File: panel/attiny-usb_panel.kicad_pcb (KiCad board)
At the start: 2 copper layers, 83 x 52.6 mm, 79 parts, among them J1 Conn_01x05, J2 Conn_01x05, J3 Conn_01x05, U1 ATtiny85-20P, U3 ATtiny85-20P, U5 ATtiny85-20P

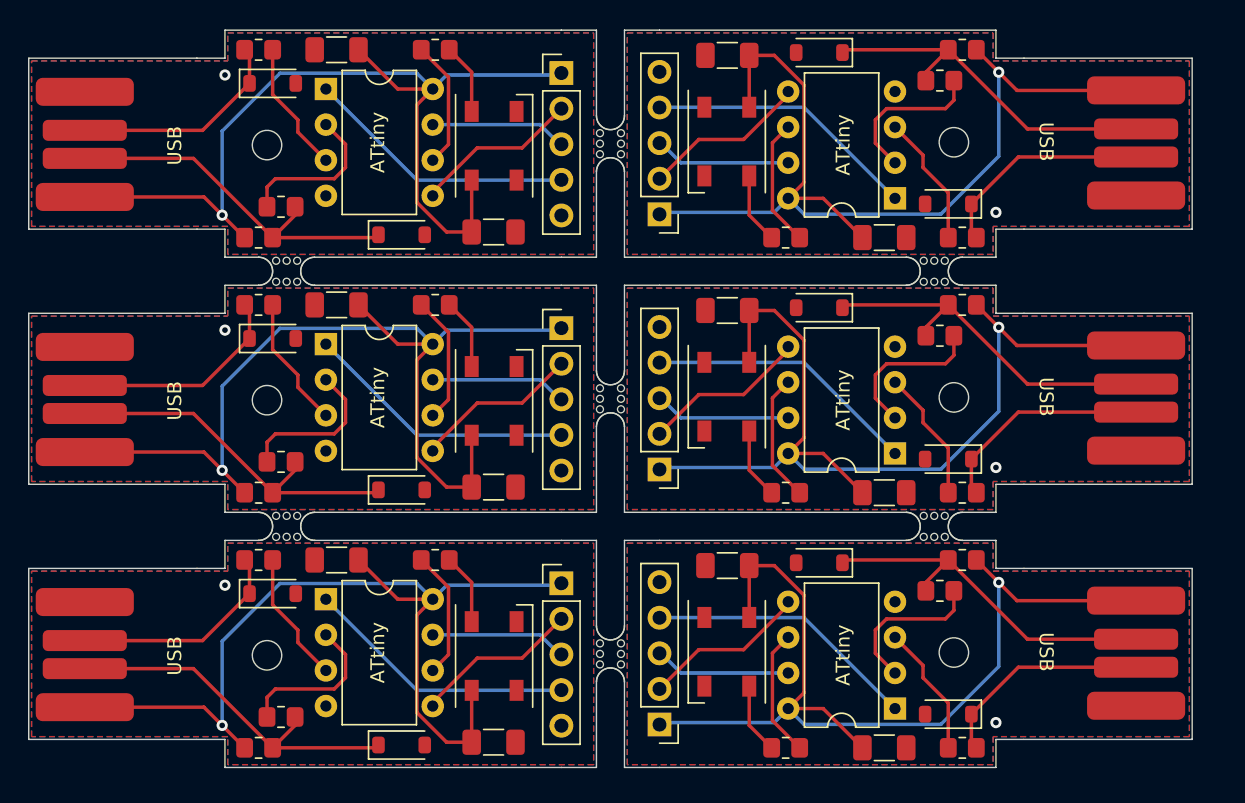
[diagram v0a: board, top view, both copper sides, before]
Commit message: create panel of 2x3
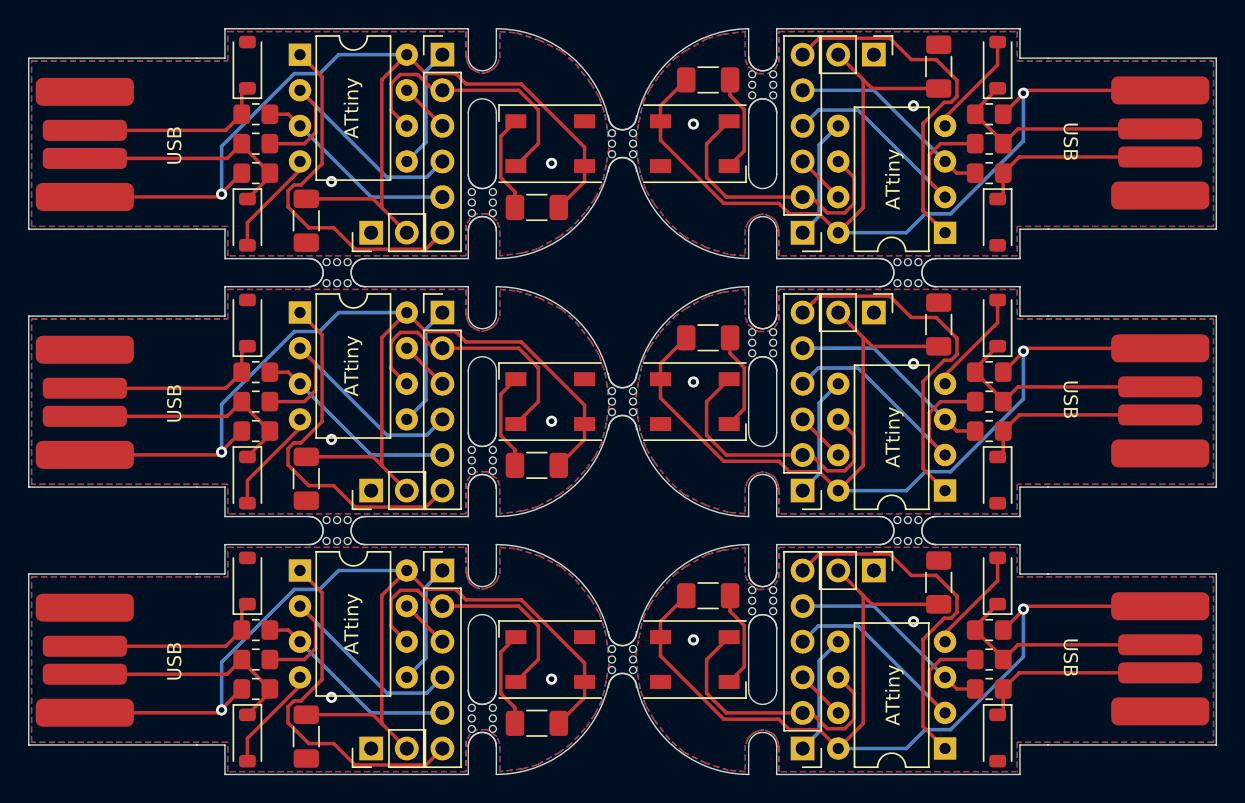
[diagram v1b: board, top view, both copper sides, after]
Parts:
- removed the C3 at (122.0, 117.6)
- removed the C3 at (161.0, 131.0)
- removed the C4 at (149.8, 118.0)
- removed the C4 at (133.2, 130.6)
- removed the C5 at (161.0, 112.8)
- removed the C5 at (122.0, 135.8)
- removed the C6 at (133.2, 148.8)
- removed the C6 at (149.8, 99.8)
- removed the D4 at (126.6, 130.8)
- removed the D4 at (156.4, 117.8)
- removed the D5 at (117.4, 120.0)
- removed the D5 at (165.6, 128.6)
- removed the D6 at (133.2, 124.5)
- removed the D6 at (149.8, 124.2)
- removed the D7 at (156.4, 99.6)
- removed the D7 at (126.6, 149.0)
- removed the D8 at (117.4, 138.2)
- removed the D8 at (165.6, 110.4)
- removed the D9 at (149.8, 106.0)
- removed the D9 at (133.2, 142.7)
- removed J1 (x2): Conn_01x05, Connector_PinHeader_2.54mm:PinHeader_1x05_P2.54mm_Vertical
- removed the J2 at (145.0, 129.3)
- removed the J2 at (138.0, 119.3)
- removed the J3 at (138.0, 137.5)
- removed the J3 at (145.0, 111.1)
- removed R10 (x2): 68R, Resistor_SMD:R_0805_2012Metric_Pad1.20x1.40mm_HandSolder
- removed R11 (x2): 400R, Resistor_SMD:R_0805_2012Metric_Pad1.20x1.40mm_HandSolder
- removed R12 (x2): 1k5, Resistor_SMD:R_0805_2012Metric_Pad1.20x1.40mm_HandSolder
- removed the R3 at (154.0, 149.2)
- removed the R3 at (129.0, 99.4)
- removed the R5 at (166.6, 131.0)
- removed the R5 at (116.4, 117.6)
- removed the R6 at (118.0, 128.8)
- removed the R6 at (165.0, 119.8)
- removed the R7 at (154.0, 131.0)
- removed the R7 at (129.0, 117.6)
- removed the R8 at (116.4, 131.0)
- removed the R8 at (166.6, 117.6)
- removed the R9 at (116.4, 135.8)
- removed the R9 at (166.6, 112.8)
- removed the U3 at (161.8, 128.2)
- removed the U3 at (121.2, 120.4)
- removed the U4 at (179.0, 124.2)
- removed the U4 at (104.0, 124.3)
- removed the U5 at (121.2, 138.6)
- removed the U5 at (161.8, 110.0)
- removed the U6 at (179.0, 106.0)
- removed the U6 at (104.0, 142.6)
- removed the mouse-bite-2mm-slot at (164.6, 115.2)
- removed the mouse-bite-2mm-slot at (141.5, 142.5)
- removed the mouse-bite-2mm-slot at (118.4, 133.4)
- removed the mouse-bite-2mm-slot at (118.4, 115.2)
- removed the mouse-bite-2mm-slot at (141.5, 106.1)
- removed the mouse-bite-2mm-slot at (141.5, 124.3)
- removed the mouse-bite-2mm-slot at (164.6, 133.4)
- added C3: 100n, Capacitor_SMD:C_1206_3216Metric_Pad1.33x1.80mm_HandSolder, F.Cu at (164.9, 119.0)
- added C3: 100n, Capacitor_SMD:C_1206_3216Metric_Pad1.33x1.80mm_HandSolder, F.Cu at (119.8, 130.0)
- added C4: 100n, Capacitor_SMD:C_1206_3216Metric_Pad1.33x1.80mm_HandSolder, F.Cu at (136.2, 129.1)
- added C4: 100n, Capacitor_SMD:C_1206_3216Metric_Pad1.33x1.80mm_HandSolder, F.Cu at (148.5, 120.0)
- added C5: 100n, Capacitor_SMD:C_1206_3216Metric_Pad1.33x1.80mm_HandSolder, F.Cu at (164.9, 100.6)
- added C5: 100n, Capacitor_SMD:C_1206_3216Metric_Pad1.33x1.80mm_HandSolder, F.Cu at (119.8, 148.4)
- added C6: 100n, Capacitor_SMD:C_1206_3216Metric_Pad1.33x1.80mm_HandSolder, F.Cu at (136.2, 147.4)
- added C6: 100n, Capacitor_SMD:C_1206_3216Metric_Pad1.33x1.80mm_HandSolder, F.Cu at (148.5, 101.5)
- added D4: 3V6, Diode_SMD:D_SOD-123, F.Cu at (115.6, 130.1)
- added D4: 3V6, Diode_SMD:D_SOD-123, F.Cu at (169.1, 118.9)
- added D5: 3V6, Diode_SMD:D_SOD-123, F.Cu at (169.1, 130.1)
- added D5: 3V6, Diode_SMD:D_SOD-123, F.Cu at (115.6, 118.9)
- added D6: WS2812B, LED_SMD:LED_SK6812_PLCC4_5.0x5.0mm_P3.2mm, F.Cu at (147.5, 124.5)
- added D6: WS2812B, LED_SMD:LED_SK6812_PLCC4_5.0x5.0mm_P3.2mm, F.Cu at (137.2, 124.5)
- added D7: 3V6, Diode_SMD:D_SOD-123, F.Cu at (169.1, 100.5)
- added D7: 3V6, Diode_SMD:D_SOD-123, F.Cu at (115.6, 148.5)
- added D8: 3V6, Diode_SMD:D_SOD-123, F.Cu at (115.6, 137.3)
- added D8: 3V6, Diode_SMD:D_SOD-123, F.Cu at (169.1, 111.7)
- added D9: WS2812B, LED_SMD:LED_SK6812_PLCC4_5.0x5.0mm_P3.2mm, F.Cu at (147.5, 106.1)
- added D9: WS2812B, LED_SMD:LED_SK6812_PLCC4_5.0x5.0mm_P3.2mm, F.Cu at (137.2, 142.9)
- added J2: Conn_01x06, Connector_PinHeader_2.54mm:PinHeader_1x06_P2.54mm_Vertical, F.Cu at (129.5, 99.8)
- added J2: Conn_01x06, Connector_PinHeader_2.54mm:PinHeader_1x06_P2.54mm_Vertical, F.Cu at (155.2, 149.2)
- added J3: Conn_01x02, Connector_PinHeader_2.54mm:PinHeader_1x02_P2.54mm_Vertical, F.Cu at (124.4, 112.5)
- added J3: Conn_01x02, Connector_PinHeader_2.54mm:PinHeader_1x02_P2.54mm_Vertical, F.Cu at (160.3, 136.6)
- added J4: Conn_01x06, Connector_PinHeader_2.54mm:PinHeader_1x06_P2.54mm_Vertical, F.Cu at (155.2, 130.8)
- added J4: Conn_01x06, Connector_PinHeader_2.54mm:PinHeader_1x06_P2.54mm_Vertical, F.Cu at (129.5, 118.2)
- added J5: Conn_01x02, Connector_PinHeader_2.54mm:PinHeader_1x02_P2.54mm_Vertical, F.Cu at (160.3, 118.2)
- added J5: Conn_01x02, Connector_PinHeader_2.54mm:PinHeader_1x02_P2.54mm_Vertical, F.Cu at (124.4, 130.8)
- added J6: Conn_01x06, Connector_PinHeader_2.54mm:PinHeader_1x06_P2.54mm_Vertical, F.Cu at (155.2, 112.5)
- added J6: Conn_01x06, Connector_PinHeader_2.54mm:PinHeader_1x06_P2.54mm_Vertical, F.Cu at (129.5, 136.6)
- added J7: Conn_01x02, Connector_PinHeader_2.54mm:PinHeader_1x02_P2.54mm_Vertical, F.Cu at (124.4, 149.2)
- added J7: Conn_01x02, Connector_PinHeader_2.54mm:PinHeader_1x02_P2.54mm_Vertical, F.Cu at (160.3, 99.8)
- added R3: 68R, Resistor_SMD:R_0805_2012Metric_Pad1.20x1.40mm_HandSolder, F.Cu at (168.5, 126.6)
- added R3: 68R, Resistor_SMD:R_0805_2012Metric_Pad1.20x1.40mm_HandSolder, F.Cu at (116.2, 122.4)
- added R5: 68R, Resistor_SMD:R_0805_2012Metric_Pad1.20x1.40mm_HandSolder, F.Cu at (116.2, 124.5)
- added R5: 68R, Resistor_SMD:R_0805_2012Metric_Pad1.20x1.40mm_HandSolder, F.Cu at (168.5, 124.5)
- added R6: 1k5, Resistor_SMD:R_0805_2012Metric_Pad1.20x1.40mm_HandSolder, F.Cu at (168.5, 122.4)
- added R6: 1k5, Resistor_SMD:R_0805_2012Metric_Pad1.20x1.40mm_HandSolder, F.Cu at (116.2, 126.6)
- added R7: 68R, Resistor_SMD:R_0805_2012Metric_Pad1.20x1.40mm_HandSolder, F.Cu at (116.2, 140.8)
- added R7: 68R, Resistor_SMD:R_0805_2012Metric_Pad1.20x1.40mm_HandSolder, F.Cu at (168.5, 108.2)
- added R8: 68R, Resistor_SMD:R_0805_2012Metric_Pad1.20x1.40mm_HandSolder, F.Cu at (168.5, 106.1)
- added R8: 68R, Resistor_SMD:R_0805_2012Metric_Pad1.20x1.40mm_HandSolder, F.Cu at (116.2, 142.9)
- added R9: 1k5, Resistor_SMD:R_0805_2012Metric_Pad1.20x1.40mm_HandSolder, F.Cu at (168.5, 104.0)
- added R9: 1k5, Resistor_SMD:R_0805_2012Metric_Pad1.20x1.40mm_HandSolder, F.Cu at (116.2, 145.0)
- added U3: ATtiny85-20P, Package_DIP:DIP-8_W7.62mm, F.Cu at (119.3, 118.2)
- added U3: ATtiny85-20P, Package_DIP:DIP-8_W7.62mm, F.Cu at (165.4, 130.8)
- added U4: ~, my_lib:pcb_usb-connector, F.Cu at (180.7, 124.5)
- added U4: ~, my_lib:pcb_usb-connector, F.Cu at (104.0, 124.5)
- added U5: ATtiny85-20P, Package_DIP:DIP-8_W7.62mm, F.Cu at (165.4, 112.5)
- added U5: ATtiny85-20P, Package_DIP:DIP-8_W7.62mm, F.Cu at (119.3, 136.6)
- added U6: ~, my_lib:pcb_usb-connector, F.Cu at (104.0, 142.9)
- added U6: ~, my_lib:pcb_usb-connector, F.Cu at (180.7, 106.0)
- added mouse-bite-2mm-slot: VAL**, my_lib:mouse-bite-2mm-slot, F.Cu at (152.4, 138.7)
- added mouse-bite-2mm-slot: VAL**, my_lib:mouse-bite-2mm-slot, F.Cu at (162.7, 115.3)
- added mouse-bite-2mm-slot: VAL**, my_lib:mouse-bite-2mm-slot, F.Cu at (132.4, 110.3)
- added mouse-bite-2mm-slot: VAL**, my_lib:mouse-bite-2mm-slot, F.Cu at (162.7, 133.7)
- added mouse-bite-2mm-slot: VAL**, my_lib:mouse-bite-2mm-slot, F.Cu at (122.0, 133.7)
- added mouse-bite-2mm-slot: VAL**, my_lib:mouse-bite-2mm-slot, F.Cu at (122.0, 115.3)
- added mouse-bite-2mm-slot: VAL**, my_lib:mouse-bite-2mm-slot, F.Cu at (142.4, 124.5)
- added mouse-bite-2mm-slot: VAL**, my_lib:mouse-bite-2mm-slot, F.Cu at (142.4, 106.1)
- added mouse-bite-2mm-slot: VAL**, my_lib:mouse-bite-2mm-slot, F.Cu at (142.4, 142.9)
- added mouse-bite-2mm-slot1: VAL**, my_lib:mouse-bite-2mm-slot, F.Cu at (132.4, 128.7)
- added mouse-bite-2mm-slot1: VAL**, my_lib:mouse-bite-2mm-slot, F.Cu at (152.4, 120.3)
- added mouse-bite-2mm-slot2: VAL**, my_lib:mouse-bite-2mm-slot, F.Cu at (132.4, 147.1)
- added mouse-bite-2mm-slot2: VAL**, my_lib:mouse-bite-2mm-slot, F.Cu at (152.4, 101.9)
- D3 (x2): value SK6812 -> WS2812B
- moved D1 12.8 mm to (169.1, 137.3), turned to 90 degrees
- moved C1 12.4 mm to (164.9, 137.4), turned to 90 degrees
- moved C1 12.4 mm to (119.8, 111.6), turned to -90 degrees
- moved D1 11.0 mm to (115.6, 111.7), turned to -90 degrees
- moved R2 6.03 mm to (168.5, 142.9), turned to 0 degrees
- moved R4 5.36 mm to (168.5, 140.8)
- moved R2 4.85 mm to (116.2, 106.1), turned to 180 degrees
- moved R1 4.62 mm to (168.5, 145.0)
- moved R1 4.60 mm to (116.2, 104.0)
- moved R4 4.60 mm to (116.2, 108.2)
- moved U1 4.57 mm to (165.4, 149.2)
- moved D3 4.00 mm to (137.2, 106.1), turned to 180 degrees
- moved D2 3.91 mm to (169.1, 148.5), turned to -90 degrees
- moved C2 3.55 mm to (136.2, 110.7), turned to 180 degrees
- moved U1 3.07 mm to (119.3, 99.8)
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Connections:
- U1 pad 6: Net-(U1-PB1) -> Net-(D3-DIN) (x2)
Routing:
- net Net-(D3-DIN): track 30.4 -> 119.9 mm
- net GND: track 0.00 -> 87.3 mm, vias 6 -> 12
- net Net-(D1-K): track 157.4 -> 102.5 mm
- net Net-(U1-PB1): track 54.9 -> 0.00 mm
- net Net-(J2-Pin_4): track 67.3 -> 121.7 mm
- net Net-(J2-Pin_6): track 116.3 -> 153.3 mm
- net Net-(J2-Pin_3): track 57.8 -> 21.6 mm
- net Net-(J2-Pin_5): track 56.7 -> 88.5 mm
- net Net-(J2-Pin_1): track 71.1 -> 52.0 mm
- net +5V: track 413.4 -> 429.4 mm
- net Net-(D2-K): track 94.1 -> 82.2 mm
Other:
- board size 83 x 52.6 mm -> 84.7 x 53.2 mm
